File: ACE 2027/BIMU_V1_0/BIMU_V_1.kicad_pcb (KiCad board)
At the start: 2 copper layers, 35 x 40.5 mm, 39 parts, among them J2 USB_C_Receptacle_USB2.0_16P, J3 UART_connector, J4 RJ45, J5 RJ45, J6 Thermal_ResistanceM, SW1 SW_Push, SW2 SW_Push, U1 ESP32-C3, U2 LSM6DS3, U3 TLV75801PDRVR, U5 ISO1050DUB, Y2 Crystal_GND24

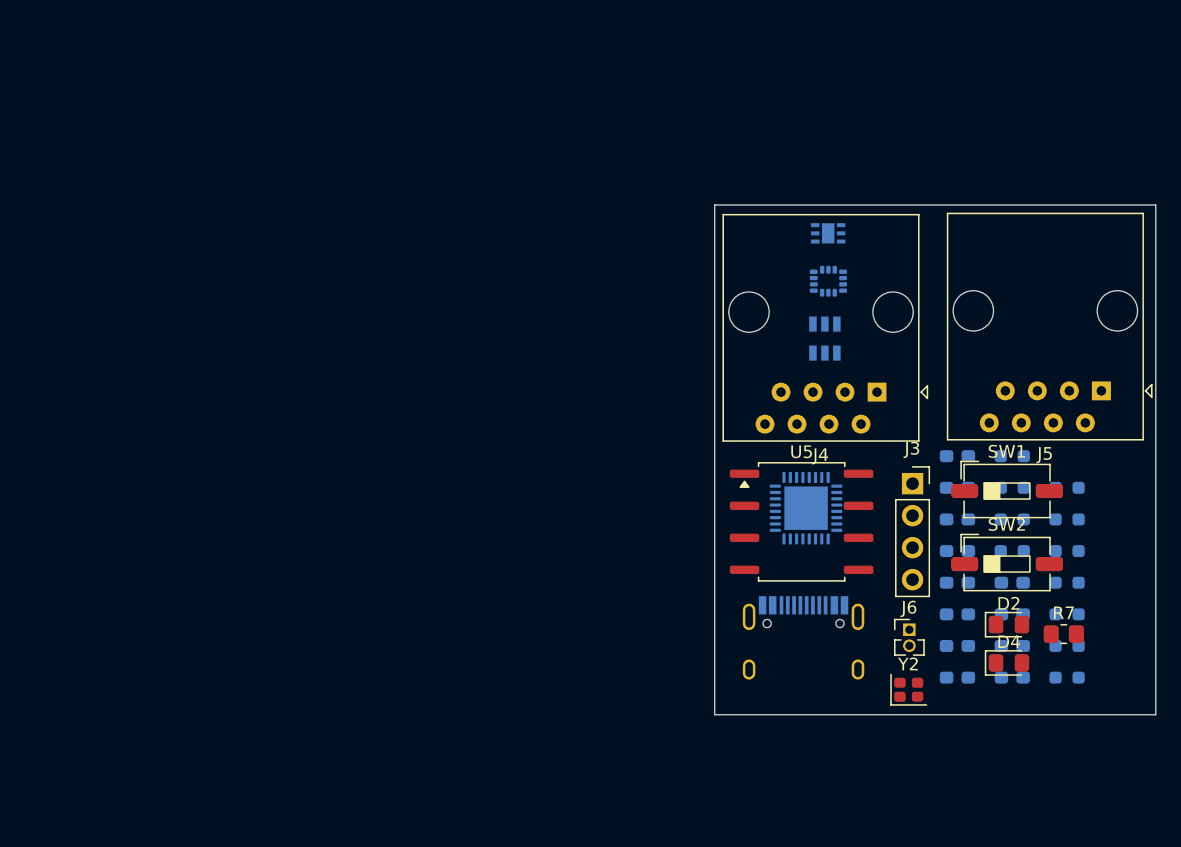
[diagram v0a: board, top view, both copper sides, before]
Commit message: Avancement of different part of the schematic
Add and reorganize numerous symbol definitions and annotations in Alimentation.kicad_sch: new TestPoint, LED, R_US/Resistor symbols, BAV99 diode, MountingHole, AP7361C-33E regulator, power/GND symbol instances, and associated symbol variants. Add global CAN_P/CAN_N labels, layout rectangles and text (ESD protection, current rating), and adjust wires/junction coordinates. Also update BIMU_V_1.kicad_pcb, BIMU_V_1.kicad_sch, Capteur.kicad_sch, Controle.kicad_sch and fp-info-cache; add several backup .zip files and a Controle.kicad_sch-bak file.
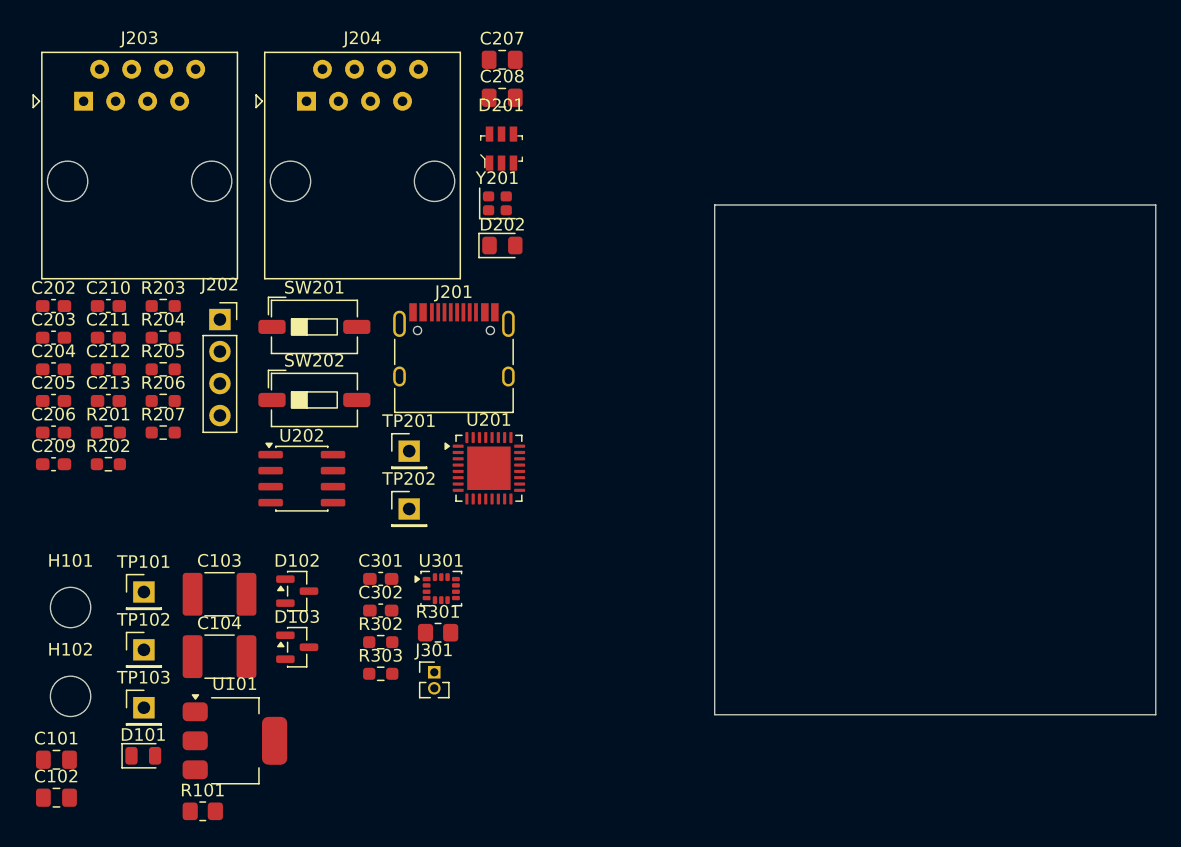
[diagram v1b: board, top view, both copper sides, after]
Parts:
- removed C10, C11, C12, C14, C15, C5, C6, C7, C9: 0.1μF, Capacitor_SMD:C_0603_1608Metric_Pad1.08x0.95mm_HandSolder
- removed C13: 22μF, Capacitor_SMD:C_0603_1608Metric_Pad1.08x0.95mm_HandSolder
- removed C16: 47nF, Capacitor_SMD:C_0603_1608Metric_Pad1.08x0.95mm_HandSolder
- removed C8: 4.7μF, Capacitor_SMD:C_0603_1608Metric_Pad1.08x0.95mm_HandSolder
- removed D1: USBLC6-2SC6, digikey-footprints:SOT23-6L
- removed D2, D4: LED POWER, LED_SMD:LED_0805_2012Metric_Pad1.15x1.40mm_HandSolder
- removed J2: USB_C_Receptacle_USB2.0_16P, Connector_USB:USB_C_Receptacle_HRO_TYPE-C-31-M-12
- removed J3: UART_connector, Connector_PinSocket_2.54mm:PinSocket_1x04_P2.54mm_Vertical
- removed J4, J5: RJ45, Connector_RJ:RJ45_Amphenol_54602-x08_Horizontal
- removed J6: Thermal_ResistanceM, Connector_PinHeader_1.27mm:PinHeader_1x02_P1.27mm_Vertical
- removed R1, R2: 5.1KΩ, Resistor_SMD:R_0603_1608Metric_Pad0.98x0.95mm_HandSolder
- removed R11, R12: 60Ω, Resistor_SMD:R_0603_1608Metric_Pad0.98x0.95mm_HandSolder
- removed R13, R8: 1.2KΩ, Resistor_SMD:R_0603_1608Metric_Pad0.98x0.95mm_HandSolder
- removed R3, R4: 10KΩ, Resistor_SMD:R_0603_1608Metric_Pad0.98x0.95mm_HandSolder
- removed R5: 2KΩ, Resistor_SMD:R_0603_1608Metric_Pad0.98x0.95mm_HandSolder
- removed R6, R9: 120Ω, Resistor_SMD:R_0603_1608Metric_Pad0.98x0.95mm_HandSolder
- removed R7: 10KΩ, Resistor_SMD:R_0805_2012Metric_Pad1.20x1.40mm_HandSolder
- removed SW1, SW2: SW_Push, Button_Switch_SMD:SW_DIP_SPSTx01_Slide_6.7x4.1mm_W6.73mm_P2.54mm_LowProfile_JPin
- removed U1: ESP32-C3, Package_DFN_QFN:QFN-32-1EP_5x5mm_P0.5mm_EP3.45x3.45mm
- removed U2: LSM6DS3, Package_LGA:LGA-14_3x2.5mm_P0.5mm_LayoutBorder3x4y
- removed U3: TLV75801PDRVR, TLV:SON65P200X200X80-7N
- removed U5: ISO1050DUB, Package_SO:SOP-8_6.62x9.15mm_P2.54mm
- removed Y2: Crystal_GND24, Crystal:Crystal_SMD_2016-4Pin_2.0x1.6mm
- added C101: 4,7µF, Capacitor_SMD:C_0805_2012Metric_Pad1.18x1.45mm_HandSolder, F.Cu at (65.4, 94.0)
- added C102: 4,7µF, Capacitor_SMD:C_0805_2012Metric_Pad1.18x1.45mm_HandSolder, F.Cu at (65.4, 97.0)
- added C103: 1nF, Capacitor_SMD:C_1812_4532Metric_Pad1.57x3.40mm_HandSolder, F.Cu at (78.3, 80.8)
- added C104: 1nF, Capacitor_SMD:C_1812_4532Metric_Pad1.57x3.40mm_HandSolder, F.Cu at (78.3, 85.8)
- added C202: 0.1μF, Capacitor_SMD:C_0603_1608Metric_Pad1.08x0.95mm_HandSolder, F.Cu at (65.1, 58.0)
- added C203: 0.1μF, Capacitor_SMD:C_0603_1608Metric_Pad1.08x0.95mm_HandSolder, F.Cu at (65.1, 60.5)
- added C204: 0.1μF, Capacitor_SMD:C_0603_1608Metric_Pad1.08x0.95mm_HandSolder, F.Cu at (65.1, 63.0)
- added C205: 0.1μF, Capacitor_SMD:C_0603_1608Metric_Pad1.08x0.95mm_HandSolder, F.Cu at (65.1, 65.5)
- added C206: 0.1μF, Capacitor_SMD:C_0603_1608Metric_Pad1.08x0.95mm_HandSolder, F.Cu at (65.1, 68.0)
- added C207: 12pF, Capacitor_SMD:C_0805_2012Metric_Pad1.18x1.45mm_HandSolder, F.Cu at (100.7, 38.4)
- added C208: 12pF, Capacitor_SMD:C_0805_2012Metric_Pad1.18x1.45mm_HandSolder, F.Cu at (100.7, 41.4)
- added C209: 0.1μF, Capacitor_SMD:C_0603_1608Metric_Pad1.08x0.95mm_HandSolder, F.Cu at (65.1, 70.5)
- added C210: 22μF, Capacitor_SMD:C_0603_1608Metric_Pad1.08x0.95mm_HandSolder, F.Cu at (69.5, 58.0)
- added C211: 0.1μF, Capacitor_SMD:C_0603_1608Metric_Pad1.08x0.95mm_HandSolder, F.Cu at (69.5, 60.5)
- added C212: 0.1μF, Capacitor_SMD:C_0603_1608Metric_Pad1.08x0.95mm_HandSolder, F.Cu at (69.5, 63.0)
- added C213: 47nF, Capacitor_SMD:C_0603_1608Metric_Pad1.08x0.95mm_HandSolder, F.Cu at (69.5, 65.5)
- added C301: 0.1μF, Capacitor_SMD:C_0603_1608Metric_Pad1.08x0.95mm_HandSolder, F.Cu at (91.1, 79.6)
- added C302: 0.1μF, Capacitor_SMD:C_0603_1608Metric_Pad1.08x0.95mm_HandSolder, F.Cu at (91.1, 82.1)
- added D101: Green_power, Diode_SMD:D_0805_2012Metric, F.Cu at (72.3, 93.7)
- added D102: BAV99, Package_TO_SOT_SMD:SOT-23, F.Cu at (84.5, 80.6)
- added D103: BAV99, Package_TO_SOT_SMD:SOT-23, F.Cu at (84.5, 85.0)
- added D201: USBLC6-2SC6, digikey-footprints:SOT23-6L, F.Cu at (100.7, 45.5)
- added D202: LED POWER, LED_SMD:LED_0805_2012Metric_Pad1.15x1.40mm_HandSolder, F.Cu at (100.8, 53.2)
- added H101: MountingHole, MountingHole:MountingHole_3.2mm_M3_ISO14580, F.Cu at (66.5, 81.9)
- added H102: MountingHole, MountingHole:MountingHole_3.2mm_M3_ISO14580, F.Cu at (66.5, 88.9)
- added J201: USB_C_Receptacle_USB2.0_16P, Connector_USB:USB_C_Receptacle_HRO_TYPE-C-31-M-12, F.Cu at (96.9, 62.5)
- added J202: UART_connector, Connector_PinSocket_2.54mm:PinSocket_1x04_P2.54mm_Vertical, F.Cu at (78.3, 59.0)
- added J203: RJ45, Connector_RJ:RJ45_Amphenol_54602-x08_Horizontal, F.Cu at (67.5, 41.7)
- added J204: RJ45, Connector_RJ:RJ45_Amphenol_54602-x08_Horizontal, F.Cu at (85.2, 41.7)
- added J301: Thermal_ResistanceM, Connector_PinHeader_1.27mm:PinHeader_1x02_P1.27mm_Vertical, F.Cu at (95.3, 87.0)
- added R101: 330Ω, Resistor_SMD:R_0805_2012Metric_Pad1.20x1.40mm_HandSolder, F.Cu at (77.0, 98.1)
- added R201: 5.1KΩ, Resistor_SMD:R_0603_1608Metric_Pad0.98x0.95mm_HandSolder, F.Cu at (69.5, 68.0)
- added R202: 5.1KΩ, Resistor_SMD:R_0603_1608Metric_Pad0.98x0.95mm_HandSolder, F.Cu at (69.5, 70.5)
- added R203: 5.1KΩ, Resistor_SMD:R_0603_1608Metric_Pad0.98x0.95mm_HandSolder, F.Cu at (73.8, 58.0)
- added R204: 5.1KΩ, Resistor_SMD:R_0603_1608Metric_Pad0.98x0.95mm_HandSolder, F.Cu at (73.8, 60.5)
- added R205: 120Ω, Resistor_SMD:R_0603_1608Metric_Pad0.98x0.95mm_HandSolder, F.Cu at (73.8, 63.0)
- added R206: 60Ω, Resistor_SMD:R_0603_1608Metric_Pad0.98x0.95mm_HandSolder, F.Cu at (73.8, 65.5)
- added R207: 60Ω, Resistor_SMD:R_0603_1608Metric_Pad0.98x0.95mm_HandSolder, F.Cu at (73.8, 68.0)
- added R301: 10KΩ, Resistor_SMD:R_0805_2012Metric_Pad1.20x1.40mm_HandSolder, F.Cu at (95.7, 83.9)
- added R302: 1.2KΩ, Resistor_SMD:R_0603_1608Metric_Pad0.98x0.95mm_HandSolder, F.Cu at (91.1, 84.6)
- added R303: 1.2KΩ, Resistor_SMD:R_0603_1608Metric_Pad0.98x0.95mm_HandSolder, F.Cu at (91.1, 87.2)
- added SW201: SW_Push, Button_Switch_SMD:SW_DIP_SPSTx01_Slide_6.7x4.1mm_W6.73mm_P2.54mm_LowProfile_JPin, F.Cu at (85.8, 59.6)
- added SW202: SW_Push, Button_Switch_SMD:SW_DIP_SPSTx01_Slide_6.7x4.1mm_W6.73mm_P2.54mm_LowProfile_JPin, F.Cu at (85.8, 65.4)
- added TP101: TP_GND_IN, Connector_PinHeader_2.54mm:PinHeader_1x01_P2.54mm_Vertical, F.Cu at (72.3, 80.7)
- added TP102: TP_5V, Connector_PinHeader_2.54mm:PinHeader_1x01_P2.54mm_Vertical, F.Cu at (72.3, 85.2)
- added TP103: TP_3v3, Connector_PinHeader_2.54mm:PinHeader_1x01_P2.54mm_Vertical, F.Cu at (72.3, 89.8)
- added TP201: TP_CAN_P, Connector_PinHeader_2.54mm:PinHeader_1x01_P2.54mm_Vertical, F.Cu at (93.4, 69.5)
- added TP202: TP_CAN_N, Connector_PinHeader_2.54mm:PinHeader_1x01_P2.54mm_Vertical, F.Cu at (93.4, 74.1)
- added U101: AP7361C-33E, Package_TO_SOT_SMD:SOT-223-3_TabPin2, F.Cu at (79.5, 92.5)
- added U201: ESP32-C3, Package_DFN_QFN:QFN-32-1EP_5x5mm_P0.5mm_EP3.45x3.45mm, F.Cu at (99.7, 70.8)
- added U202: SN65HVD232DR, Package_SO:SOIC-8_3.9x4.9mm_P1.27mm, F.Cu at (84.8, 71.7)
- added U301: LSM6DS3, Package_LGA:LGA-14_3x2.5mm_P0.5mm_LayoutBorder3x4y, F.Cu at (95.9, 80.4)
- added Y201: ABM8-40.000MHZ-10-D1G-T, Crystal:Crystal_SMD_2016-4Pin_2.0x1.6mm, F.Cu at (100.4, 49.8)
